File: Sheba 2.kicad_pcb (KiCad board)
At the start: 2 copper layers, 85.7 x 54 mm, 63 parts, among them J2 Conn_01x03_Pin, J3 Conn_01x03_Pin, J4 Conn_01x03_Pin, J7 Conn_01x06_Pin, J8 Conn_01x02_Pin, J9 Conn_02x04_Top_Bottom, P1 USB_C_Plug_USB2.0, SW1 SW_SPDT, U1 AP62300TWU, U3 MIC5504-3.3YM5, U4 STM32F072CBTx

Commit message: Actually get ready to add protections
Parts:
- renumbered C2 to C1, C19 to C10, C6 to C11, C3 to C12, C5 to C13, C16 to C14, C7 to C15, C18 to C16, C4 to C2, C14 to C3, C17 to C4, C10 to C5, C12 to C6, C1 to C7, C13 to C9, D8 to D1, D7 to D2, D1 to D3, D2 to D4, D3 to D5, D4 to D6, D5 to D7, D6 to D8, EP3 to EP1, EP1 to EP2, EP2 to EP3, H3 to H2, H2 to H3, J8 to J1, J9 to J2, J7 to J3, J3 to J5, J2 to J6, R14 to R1, R9 to R10, R10 to R11, R11 to R12, R1 to R2, R13 to R3, R12 to R4, R3 to R5, R2 to R6, R6 to R7, R7 to R8, R8 to R9, U4 to U1, U3 to U2, U1 to U3
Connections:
- net /M1_OUT1 renamed /Power & Motors/M1_OUT1
- net /M1_OUT2 renamed /Power & Motors/M1_OUT2
- net /M2_OUT1 renamed /Power & Motors/M2_OUT1
- net /M2_OUT2 renamed /Power & Motors/M2_OUT2
- net /M3_OUT1 renamed /Power & Motors/M3_OUT1
- net /M3_OUT2 renamed /Power & Motors/M3_OUT2
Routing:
- net GND: track 41.9 -> 49.8 mm, vias 3 -> 5

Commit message: Ready to finalize Rev3
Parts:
- added D10: D_Zener3.3V, Diode_SMD:D_SOD-123, B.Cu at (117.2, 57.7)
- added D11: D_Zener5V, Diode_SMD:D_SOD-123, B.Cu at (77.5, 51.6)
- added D12: D_Zener5V, Diode_SMD:D_SOD-123, B.Cu at (74.9, 51.6)
- added D9: D_Zener3.3V, Diode_SMD:D_SOD-123, B.Cu at (117.2, 55.1)
- moved SW1 2.29 mm to (99.2, 58.9)
- moved J3 0.37 mm to (121.9, 57.9)
- moved J2 0.11 mm to (127.0, 37.6)
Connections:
- U1 pad 4: GPIO5 -> GPIO0
- U1 pad 42: GPIO0 -> GPIO5
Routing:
- net GPIO5: track 28.8 -> 21.7 mm, vias 2 -> 0
- net GPIO0: track 19.7 -> 24.6 mm, vias 0 -> 2
- net GND: track 49.8 -> 51.2 mm, vias 5 -> 7
- net KIWI_DRIVE: track 9.77 -> 11.0 mm
- net SYS_SWDIO: track 11.9 -> 10.9 mm
- net M1_FWD: track 10.2 -> 9.44 mm
- net USB_D-: track 28.7 -> 28.0 mm
- net USB_D+: track 29.4 -> 28.6 mm
- net M1_REV: track 12.5 -> 11.9 mm
- net +5V: vias 2 -> 4
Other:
- board text added: "Brian Jia"
- board text added: "Designed by"
- board text added: "Drew Straub"
- board text added: "Griffin Bohm"
- board text added: "Sam Patterson"
- board text added: "Wouldn't be"
- board text added: "possible"
- board text added: "without:"
- board text removed: "3.3V"
- board text removed: "Designed by Brian Jia Wouldn't be possible without: Griffin Bohm Sam Patterson Drew Straub"

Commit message: Rev3 ready to order
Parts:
- C7: value C0.1uF -> C1uF
- C8: value C10uF -> C22uF
- P1: value USB_C_Plug_USB2.0 -> USB 2.0 Type-C Port
- SW1: value SW_SPDT -> SPDT Switch

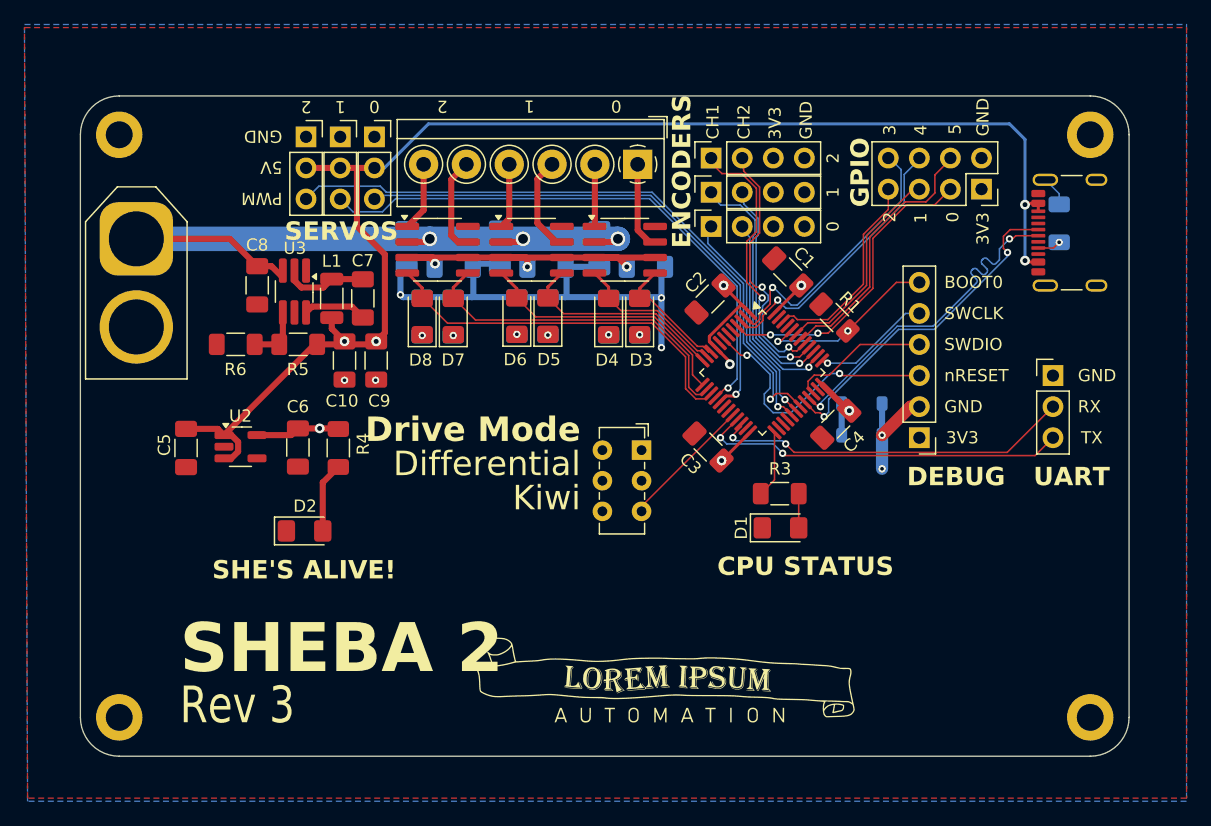
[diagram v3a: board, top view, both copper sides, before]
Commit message: Rewire the entire thing to use hardware PWM and software quadrature decoding
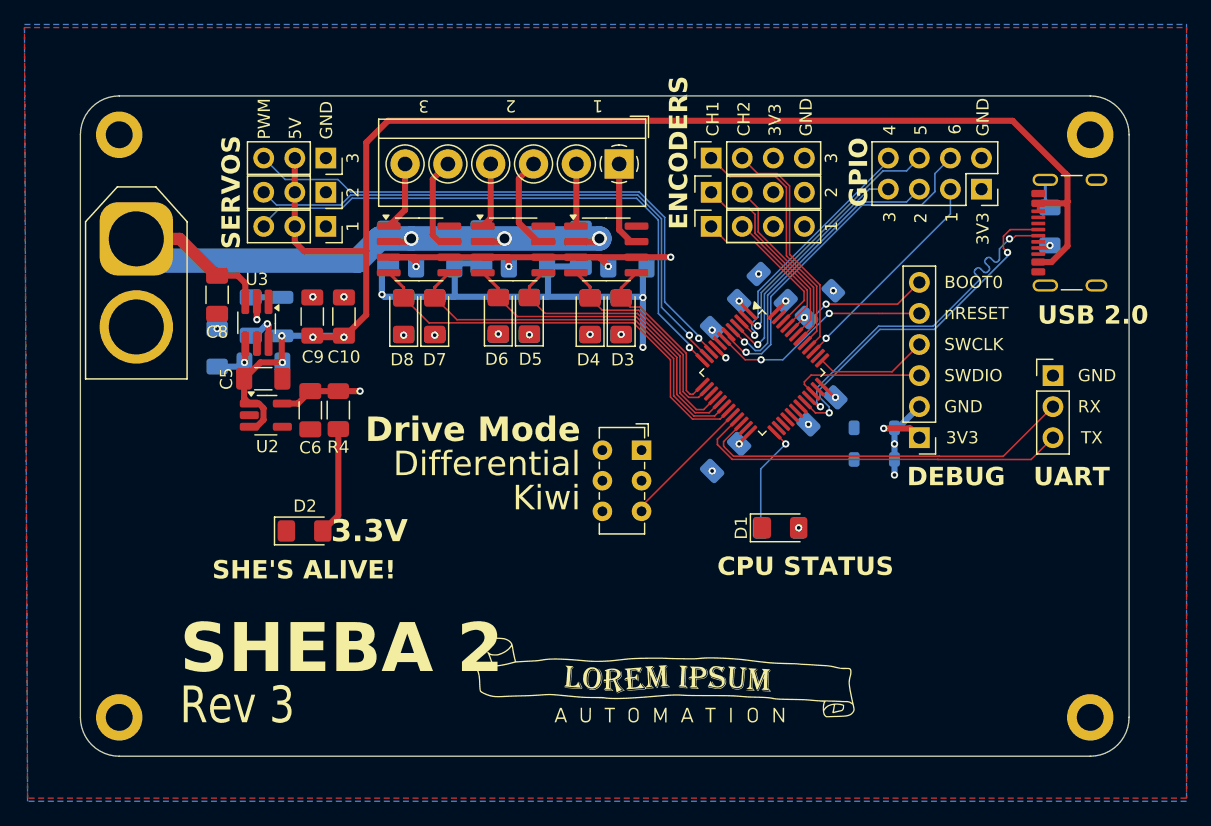
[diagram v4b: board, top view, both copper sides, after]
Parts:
- C1, C2, C3, C4, C7, L1, R1, R3, R5, R6: moved to B.Cu
- moved C7 9.29 mm to (67.3, 48.0)
- moved C5 8.48 mm to (68.3, 53.1), turned to 0 degrees
- moved J5 7.42 mm to (73.4, 40.6), turned to -90 degrees
- moved C9 6.34 mm to (72.3, 48.0), turned to 90 degrees
- moved D11 6.22 mm to (72.3, 48.0), turned to 90 degrees
- moved J4 6.02 mm to (73.4, 37.8), turned to -90 degrees
- moved L1 4.35 mm to (69.8, 48.0)
- moved U3 3.99 mm to (67.8, 48.5)
- moved C10 3.59 mm to (74.9, 48.0), turned to 90 degrees
- moved D12 3.52 mm to (74.9, 48.0), turned to 90 degrees
- moved C8 3.37 mm to (64.5, 46.2)
- moved U2 3.31 mm to (68.5, 56.1)
- moved R5 3.23 mm to (68.3, 51.8)
- moved C6 3.21 mm to (72.1, 55.7)
- moved R4 3.10 mm to (74.4, 55.7)
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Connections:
- EP1 pad 1: TIM1_CH1 -> ENC1_1
- EP1 pad 2: TIM1_CH2 -> ENC1_2
- EP2 pad 1: TIM2_CH1 -> ENC2_1
- EP2 pad 2: TIM2_CH2 -> ENC2_2
- EP3 pad 1: TIM3_CH1 -> ENC3_1
- EP3 pad 2: TIM3_CH2 -> ENC3_2
- J2 pad 3: GPIO0 -> GPIO1
- J2 pad 4: GPIO5 -> GPIO6
- J2 pad 5: GPIO1 -> GPIO2
- J2 pad 6: GPIO4 -> GPIO5
- J2 pad 7: GPIO2 -> GPIO3
- J2 pad 8: GPIO3 -> GPIO4
- J3 pad 3: NRST -> SYS_SWDIO
- J3 pad 4: SYS_SWDIO -> SYS_SWCLK
- J3 pad 5: SYS_SWCLK -> NRST
- J4 pad 3: SERVO0 -> SERVO2
- J5 pad 3: SERVO1 -> SERVO3
- J6 pad 3: SERVO2 -> SERVO1
- U1 pad 10: M1_FWD -> SERVO1
- U1 pad 11: M1_REV -> SERVO2
- U1 pad 12: M2_FWD -> SERVO3
- U1 pad 13: M2_REV -> M1_FWD
- U1 pad 14: M3_FWD -> M1_REV
- U1 pad 15: M3_REV -> unconnected-(U1-PA5-Pad15)
- U1 pad 16: SERVO1 -> M2_FWD
- U1 pad 17: SERVO0 -> M2_REV
- U1 pad 18: unconnected-(U1-PB0-Pad18) -> M3_FWD
- U1 pad 19: unconnected-(U1-PB1-Pad19) -> M3_REV
- U1 pad 2: GPIO3 -> GPIO5
- U1 pad 29: TIM1_CH1 -> unconnected-(U1-PA8-Pad29)
- U1 pad 30: TIM1_CH2 -> unconnected-(U1-PA9-Pad30)
- U1 pad 31: SERVO2 -> unconnected-(U1-PA10-Pad31)
- U1 pad 38: TIM2_CH1 -> unconnected-(U1-PA15-Pad38)
- U1 pad 39: TIM2_CH2 -> GPIO1
- U1 pad 4: GPIO0 -> GPIO3
- U1 pad 40: TIM3_CH1 -> ENC3_2
- U1 pad 41: TIM3_CH2 -> ENC3_1
- U1 pad 42: GPIO5 -> ENC2_2
- U1 pad 43: GPIO1 -> ENC2_1
- U1 pad 45: unconnected-(U1-PB8-Pad45) -> ENC1_2
- U1 pad 46: GPIO2 -> ENC1_1
- U1 pad 5: unconnected-(U1-PF0-Pad5) -> GPIO2
- U1 pad 6: unconnected-(U1-PF1-Pad6) -> GPIO6
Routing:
- net SERVO3: track 0.00 -> 46.9 mm, vias 0 -> 1
- net SERVO0: track 43.3 -> 0.00 mm, vias 1 -> 0
- net GPIO6: track 0.00 -> 28.7 mm, vias 0 -> 1
- net GPIO0: track 24.6 -> 0.00 mm, vias 2 -> 0
- net TIM3_CH1: track 22.5 -> 0.00 mm, vias 2 -> 0
- net TIM2_CH1: track 21.5 -> 0.00 mm, vias 1 -> 0
- net ENC3_1: track 0.00 -> 21.3 mm
- net TIM3_CH2: track 21.0 -> 0.00 mm, vias 2 -> 0
- net ENC3_2: track 0.00 -> 19.4 mm
- net TIM1_CH1: track 18.5 -> 0.00 mm, vias 1 -> 0
- net TIM2_CH2: track 18.4 -> 0.00 mm, vias 1 -> 0
- net TIM1_CH2: track 17.0 -> 0.00 mm, vias 1 -> 0
- net ENC2_1: track 0.00 -> 16.5 mm
- net ENC2_2: track 0.00 -> 14.8 mm
- net ENC1_1: track 0.00 -> 13.0 mm
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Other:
- board text added: "3.3V"
- board text added: "6"
- board text added: "USB 2.0"
- board text removed: "0"
